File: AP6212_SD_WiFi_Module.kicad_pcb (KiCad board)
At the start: 2 copper layers, 24.6 x 23.7 mm, 21 parts, among them J1 Conn_Coaxial, J2 TF_Card, U1 AP6212, Y1 26MHz

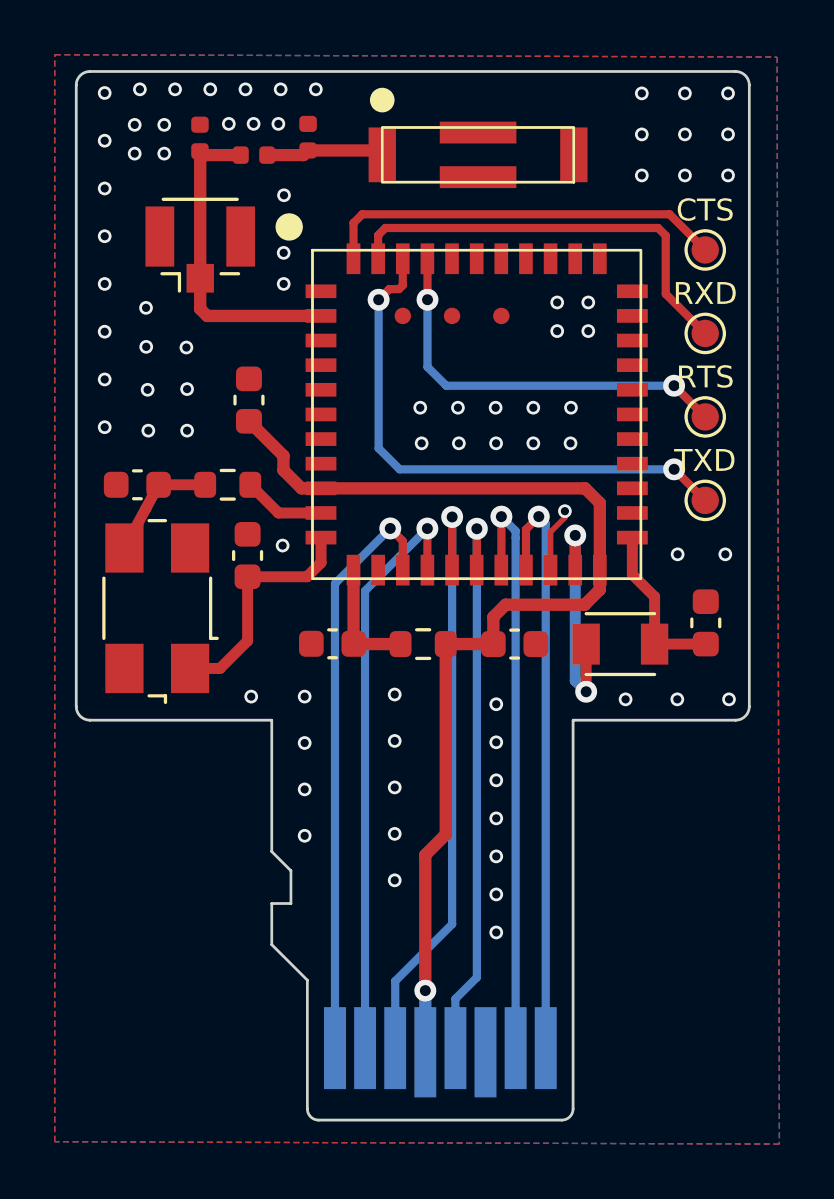
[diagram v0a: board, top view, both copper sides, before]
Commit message: feat: Change the crystal package to SMD 3225
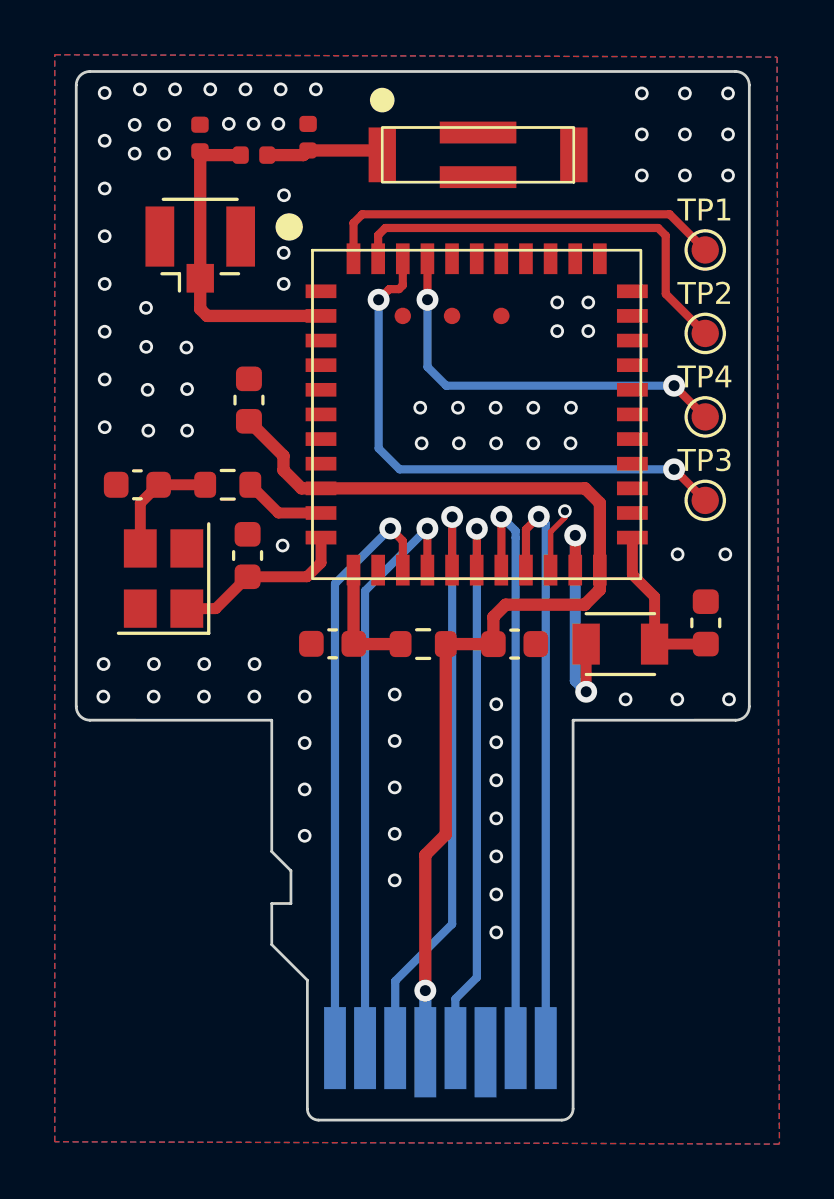
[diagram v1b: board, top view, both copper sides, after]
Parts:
- Y1: footprint Crystal:Crystal_SMD_0603-4Pin_6.0x3.5mm -> Crystal:Crystal_SMD_3225-4Pin_3.2x2.5mm
- moved Y1 1.11 mm to (200.9, 124.8)
- renumbered CTS to TP1, RXD to TP2, TXD to TP3, RTS to TP4
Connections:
- U1 pad 45: (no net) -> unconnected-(U1-TP1-Pad45)
- U1 pad 46: (no net) -> unconnected-(U1-TP2-Pad46)
- U1 pad 47: (no net) -> unconnected-(U1-TP3/NC-Pad47)
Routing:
- net Net-(U1-XTAL_OUT): track 8.67 -> 6.52 mm
- net GND: vias 78 -> 85

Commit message: feat: Fixed test point silkscreen
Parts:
- renumbered TP1 to CTS, TP4 to RTS, TP2 to RXD, TP3 to TXD
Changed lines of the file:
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@@
     (property "ki_keywords" "test point tp")
     (attr exclude_from_pos_files)
-    (fp_text reference "TP2" (at 0 -1.448) (layer "F.SilkS")
+    (fp_text reference "RXD" (at 0 -1.448) (layer "F.SilkS")
         (effects (font (size 0.8 0.8) (thickness 0.15)))
     )
@@
     (property "ki_keywords" "test point tp")
     (attr exclude_from_pos_files)
-    (fp_text reference "TP1" (at 0 -1.448) (layer "F.SilkS")
+    (fp_text reference "CTS" (at 0 -1.448) (layer "F.SilkS")
         (effects (font (size 0.8 0.8) (thickness 0.15)))
     )
@@
     (property "ki_keywords" "test point tp")
     (attr exclude_from_pos_files)
-    (fp_text reference "TP3" (at 0 -1.448) (layer "F.SilkS")
+    (fp_text reference "TXD" (at 0 -1.448) (layer "F.SilkS")
         (effects (font (size 0.8 0.8) (thickness 0.15)))
     )
@@
     (property "ki_keywords" "test point tp")
     (attr exclude_from_pos_files)
-    (fp_text reference "TP4" (at 0 -1.448) (layer "F.SilkS")
+    (fp_text reference "RTS" (at 0 -1.448) (layer "F.SilkS")
         (effects (font (size 0.8 0.8) (thickness 0.15)))
     )

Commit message: feat: Components layout adjustment
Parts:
- moved C2 1.55 mm to (204.0, 125.5), turned to 90 degrees
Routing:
- net GND: vias 85 -> 86
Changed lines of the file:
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@@
   )
   (footprint "Capacitor_SMD:C_0603_1608Metric" (layer "F.Cu")
-    (at 203.97 123.985 -90)
+    (at 203.97 125.535 90)
     (descr "Capacitor SMD 0603 (1608 Metric), square (rectangular) end terminal, IPC_7351 nominal, (Body size source: IPC-SM-782 page 76, https://www.pcb-3d.com/wordpress/wp-content/uploads/ipc-sm-782a_amendment_1_and_2.pdf), generated with kicad-footprint-generator")
     (tags "capacitor")
@@
     (fp_line (start 0.8 0.4) (end -0.8 0.4)
       (stroke (width 0.1) (type solid)) (layer "F.Fab"))
-    (pad "1" smd roundrect (at -0.775 0 270) (size 0.9 0.95) (layers "F.Cu" "F.Paste" "F.Mask") (roundrect_rratio 0.25)
+    (pad "1" smd roundrect (at -0.775 0 90) (size 0.9 0.95) (layers "F.Cu" "F.Paste" "F.Mask") (roundrect_rratio 0.25)
       (net 10 "GND") (pintype "passive"))
-    (pad "2" smd roundrect (at 0.775 0 270) (size 0.9 0.95) (layers "F.Cu" "F.Paste" "F.Mask") (roundrect_rratio 0.25)
+    (pad "2" smd roundrect (at 0.775 0 90) (size 0.9 0.95) (layers "F.Cu" "F.Paste" "F.Mask") (roundrect_rratio 0.25)
       (net 25 "Net-(U1-XTAL_OUT)") (pintype "passive"))
     (model "${KICAD6_3DMODEL_DIR}/Capacitor_SMD.3dshapes/C_0603_1608Metric.wrl"
@@
   (via (at 216.417 114.739) (size 0.5) (drill 0.3) (layers "F.Cu" "B.Cu") (free) (net 10))
   (via (at 218.373 110.098) (size 0.5) (drill 0.3) (layers "F.Cu" "B.Cu") (free) (net 10))
+  (via (at 203.96 123.12) (size 0.5) (drill 0.3) (layers "F.Cu" "B.Cu") (free) (net 10))
   (via (at 199.845 109.301) (size 0.5) (drill 0.3) (layers "F.Cu" "B.Cu") (free) (net 10))
   (via (at 205.25 123.62) (size 0.5) (drill 0.3) (layers "F.Cu" "B.Cu") (free) (net 10))

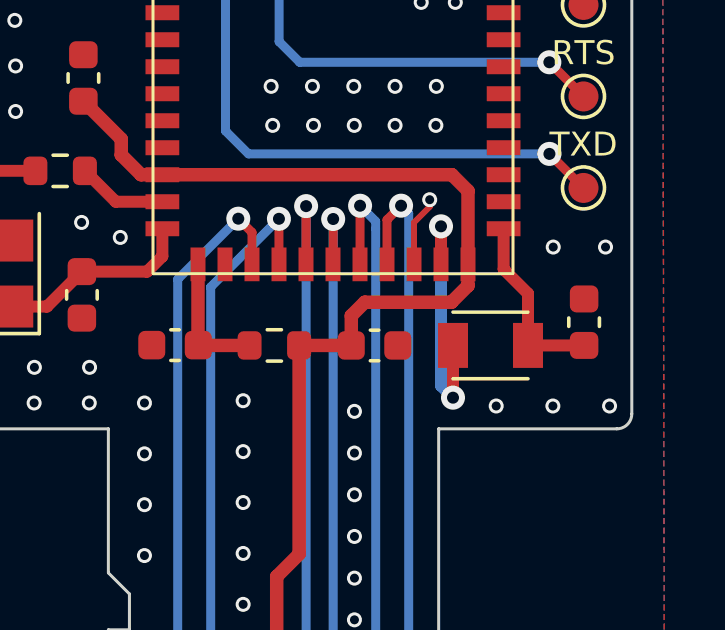
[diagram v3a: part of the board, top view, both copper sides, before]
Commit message: feat: Set constraint rules and fine-tune layout
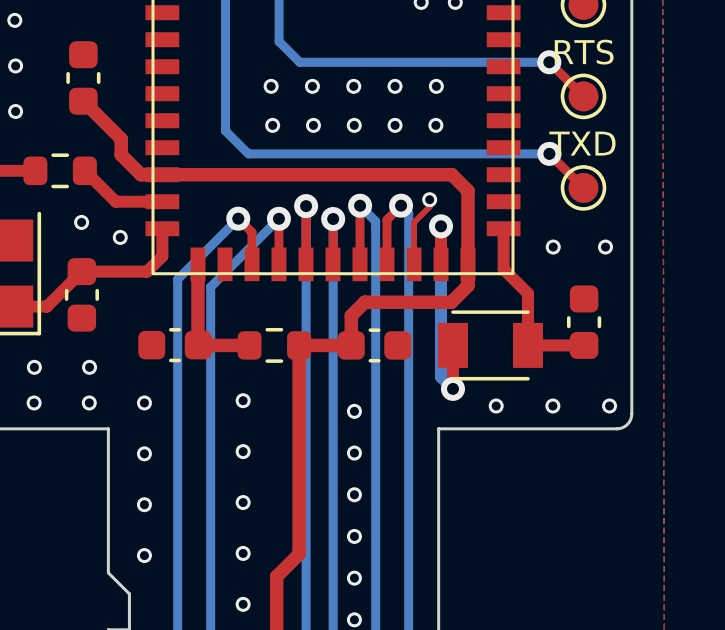
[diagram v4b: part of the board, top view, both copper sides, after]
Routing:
- net Net-(U1-VIN_LDO_OUT): track 8.89 -> 8.30 mm
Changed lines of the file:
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@@
   (segment (start 206.6525 115.23) (end 202.491 115.23) (width 0.45) (layer "F.Cu") (net 11))
   (segment (start 215.94 124.5175) (end 215.94 123.25) (width 0.4) (layer "F.Cu") (net 12))
-  (segment (start 216.34 127.22) (end 216.34 128.961) (width 0.4) (layer "F.Cu") (net 12))
+  (segment (start 216.34 127.22) (end 216.34 128.67) (width 0.4) (layer "F.Cu") (net 12))
   (via (at 215.94 123.25) (size 0.8) (drill 0.4) (layers "F.Cu" "B.Cu") (net 12))
-  (via (at 216.34 128.961) (size 0.8) (drill 0.4) (layers "F.Cu" "B.Cu") (net 12))
-  (segment (start 215.94 128.561) (end 216.34 128.961) (width 0.4) (layer "B.Cu") (net 12))
-  (segment (start 215.94 123.25) (end 215.94 128.561) (width 0.4) (layer "B.Cu") (net 12))
+  (via (at 216.34 128.67) (size 0.8) (drill 0.4) (layers "F.Cu" "B.Cu") (net 12))
+  (segment (start 215.94 128.27) (end 216.34 128.67) (width 0.4) (layer "B.Cu") (net 12))
+  (segment (start 215.94 123.25) (end 215.94 128.27) (width 0.4) (layer "B.Cu") (net 12))
   (segment (start 218.84 125.491) (end 218.0275 124.6785) (width 0.4) (layer "F.Cu") (net 13))
   (segment (start 218.84 127.22) (end 218.84 125.491) (width 0.4) (layer "F.Cu") (net 13))
@@
   )
   (zone (net 10) (net_name "GND") (layers "F&B.Cu") (hatch edge 0.5)
-    (connect_pads yes (clearance 0.25))
-    (min_thickness 0.25) (filled_areas_thickness no)
+    (connect_pads yes (clearance 0.3))
+    (min_thickness 0.3) (filled_areas_thickness no)
     (fill yes (thermal_gap 0.5) (thermal_bridge_width 0.5))
     (polygon
@@
       )
     )
+  )
+  (zone (net 0) (net_name "") (layer "B.Cu") (hatch edge 0.5)
+    (connect_pads yes (clearance 0))
+    (min_thickness 0.3) (filled_areas_thickness no)
+    (keepout (tracks allowed) (vias allowed) (pads allowed) (copperpour not_allowed) (footprints allowed))
+    (fill (thermal_gap 0.5) (thermal_bridge_width 0.5))
+    (polygon
+      (pts
+        (xy 215.85 129.8)
+        (xy 215.3 129.8)
+        (xy 215.3 140.28)
+        (xy 215.86 140.28)
+      )
+    )
+  )
+  (zone (net 0) (net_name "") (layer "B.Cu") (hatch edge 0.5)
+    (connect_pads yes (clearance 0))
+    (min_thickness 0.3) (filled_areas_thickness no)
+    (keepout (tracks allowed) (vias allowed) (pads allowed) (copperpour not_allowed) (footprints allowed))
+    (fill (thermal_gap 0.5) (thermal_bridge_width 0.5))
+    (polygon
+      (pts
+        (xy 206.35 143.48)
+        (xy 215.67 143.48)
+        (xy 215.67 144.42)
+        (xy 206.35 144.42)
+      )
+    )

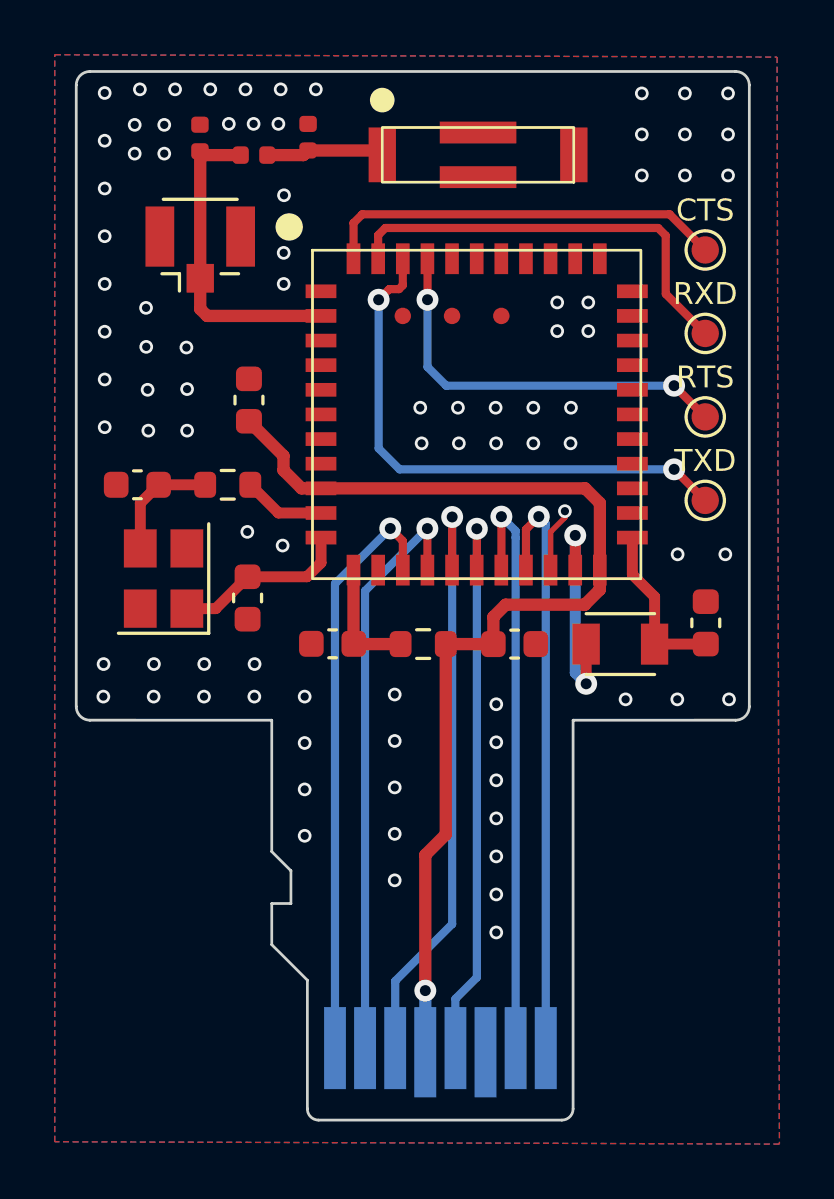
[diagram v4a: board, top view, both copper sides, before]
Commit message: feat: Optimized layout and routing
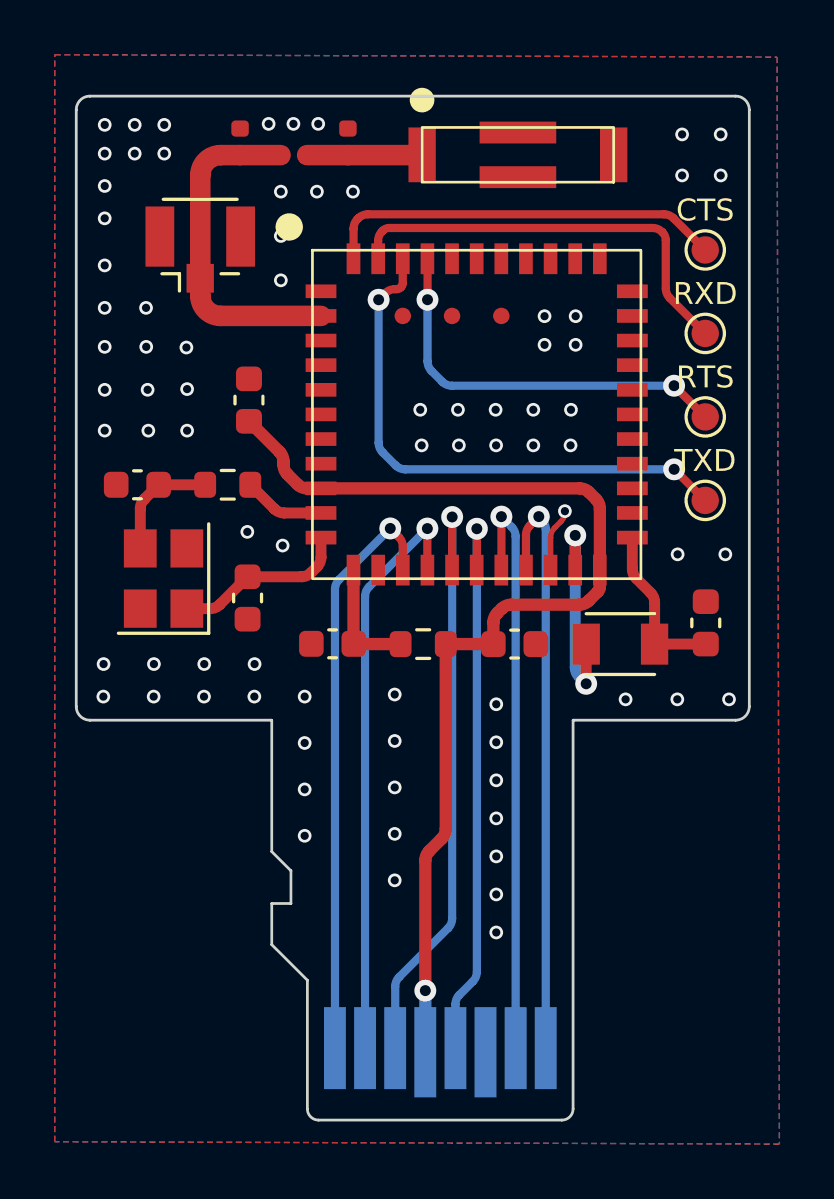
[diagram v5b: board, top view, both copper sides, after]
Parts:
- moved L3 1.47 mm to (203.7, 108.9)
- moved L2 1.46 mm to (207.6, 108.9)
- moved AE1 1.46 mm to (213.8, 109.3)
- moved L1 1.45 mm to (205.7, 109.4)
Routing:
- net Net-(J1-In): track 11.8 -> 12.5 mm
- net GND: track 2.37 -> 2.32 mm, vias 86 -> 78
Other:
- board size 24.6 x 23.7 mm -> 24.6 x 22.8 mm

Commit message: feat: Determine the final pcb shape and adjust part of the gnd hole position
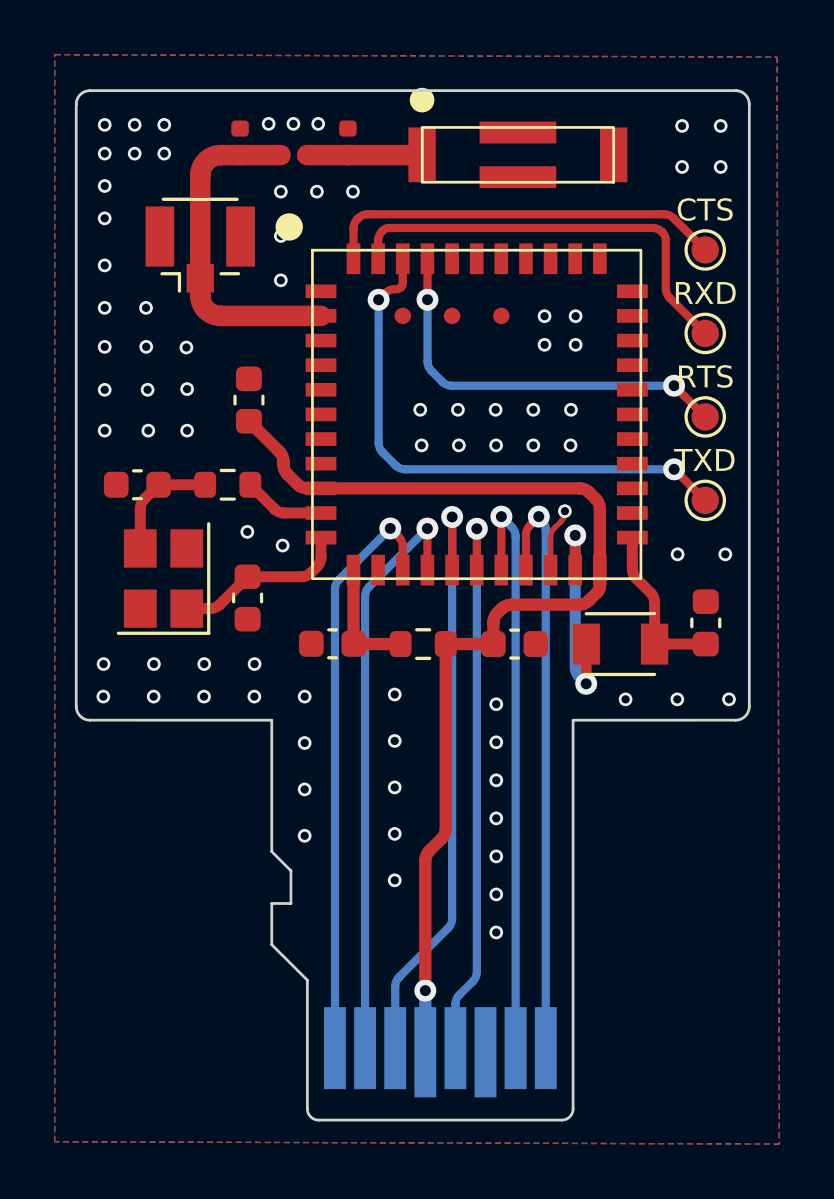
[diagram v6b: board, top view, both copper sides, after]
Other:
- board size 24.6 x 22.8 mm -> 24.6 x 23 mm
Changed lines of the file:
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@@
   (gr_line (start 198.21 130) (end 204.853 130.0005)
     (stroke (width 0.1) (type default)) (layer "Edge.Cuts"))
-  (gr_line (start 197.71 107.7) (end 197.71 129.5)
+  (gr_line (start 197.71 107.5) (end 197.71 129.5)
     (stroke (width 0.1) (type default)) (layer "Edge.Cuts"))
-  (gr_line (start 222.3 129.5) (end 222.3 107.7)
+  (gr_line (start 222.3 129.5) (end 222.3 107.5)
     (stroke (width 0.1) (type default)) (layer "Edge.Cuts"))
   (gr_line (start 221.8 130) (end 215.862 130.0005)
     (stroke (width 0.1) (type default)) (layer "Edge.Cuts"))
-  (gr_arc (start 197.71 107.7) (mid 197.856446 107.346446) (end 198.21 107.2)
+  (gr_arc (start 197.71 107.5) (mid 197.856446 107.146446) (end 198.21 107)
     (stroke (width 0.1) (type default)) (layer "Edge.Cuts"))
-  (gr_arc (start 221.8 107.2) (mid 222.153554 107.346446) (end 222.3 107.7)
+  (gr_arc (start 221.8 107) (mid 222.153554 107.146446) (end 222.3 107.5)
     (stroke (width 0.1) (type default)) (layer "Edge.Cuts"))
-  (gr_line (start 221.8 107.2) (end 198.21 107.2)
+  (gr_line (start 221.8 107) (end 198.21 107)
     (stroke (width 0.1) (type default)) (layer "Edge.Cuts"))
   (gr_arc (start 222.3 129.5) (mid 222.153553 129.853553) (end 221.8 130)
@@
   (via (at 198.75 110.483) (size 0.5) (drill 0.3) (layers "F.Cu" "B.Cu") (free) (net 10))
   (via (at 198.7 129.138) (size 0.5) (drill 0.3) (layers "F.Cu" "B.Cu") (free) (net 10))
-  (via (at 219.845 110.098) (size 0.5) (drill 0.3) (layers "F.Cu" "B.Cu") (free) (net 10))
+  (via (at 219.845 109.789) (size 0.5) (drill 0.3) (layers "F.Cu" "B.Cu") (free) (net 10))
   (via (at 206.055 130.833333) (size 0.5) (drill 0.3) (layers "F.Cu" "B.Cu") (free) (net 10))
   (via (at 200.925 108.25) (size 0.5) (drill 0.3) (layers "F.Cu" "B.Cu") (free) (net 10))
@@
   (via (at 201.734 116.385) (size 0.5) (drill 0.3) (layers "F.Cu" "B.Cu") (free) (net 10))
   (via (at 206.5025 110.69) (size 0.5) (drill 0.3) (layers "F.Cu" "B.Cu") (free) (net 10))
-  (via (at 219.845 108.599) (size 0.5) (drill 0.3) (layers "F.Cu" "B.Cu") (free) (net 10))
+  (via (at 219.845 108.29) (size 0.5) (drill 0.3) (layers "F.Cu" "B.Cu") (free) (net 10))
   (via (at 198.70875 127.95) (size 0.5) (drill 0.3) (layers "F.Cu" "B.Cu") (free) (net 10))
   (via (at 198.75 108.25) (size 0.5) (drill 0.3) (layers "F.Cu" "B.Cu") (free) (net 10))
@@
   (via (at 213.055 130.807699) (size 0.5) (drill 0.3) (layers "F.Cu" "B.Cu") (net 10))
   (via (at 209.345 130.75925) (size 0.5) (drill 0.3) (layers "F.Cu" "B.Cu") (free) (net 10))
-  (via (at 221.255 108.599) (size 0.5) (drill 0.3) (layers "F.Cu" "B.Cu") (free) (net 10))
+  (via (at 221.255 108.29) (size 0.5) (drill 0.3) (layers "F.Cu" "B.Cu") (free) (net 10))
   (via (at 214.819 116.286) (size 0.5) (drill 0.3) (layers "F.Cu" "B.Cu") (free) (net 10))
   (via (at 205.6445 108.214) (size 0.5) (drill 0.3) (layers "F.Cu" "B.Cu") (free) (net 10))
@@
   (via (at 200.259 114.936) (size 0.5) (drill 0.3) (layers "F.Cu" "B.Cu") (free) (net 10))
   (via (at 213.055 132.197398) (size 0.5) (drill 0.3) (layers "F.Cu" "B.Cu") (net 10))
-  (via (at 221.255 110.098) (size 0.5) (drill 0.3) (layers "F.Cu" "B.Cu") (free) (net 10))
+  (via (at 221.255 109.789) (size 0.5) (drill 0.3) (layers "F.Cu" "B.Cu") (free) (net 10))
   (via (at 200.5475 127.95) (size 0.5) (drill 0.3) (layers "F.Cu" "B.Cu") (free) (net 10))
   (via (at 211.65475 118.659) (size 0.5) (drill 0.3) (layers "F.Cu" "B.Cu") (free) (net 10))
